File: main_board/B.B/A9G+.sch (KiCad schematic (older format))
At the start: 20 parts

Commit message: preparation_to_drawing_PCB
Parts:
- removed Q? (x2): Q_NMOS_DGS, Package_TO_SOT_SMD:SOT-23, symbol Device:Q_NMOS_DGS
- added Q? (x2): CJ3134K, Package_TO_SOT_SMD:SOT-23, symbol Transistor_FET:2N7002
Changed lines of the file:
@@
 Text HLabel 2150 3550 0    50   Input ~ 0
 PWR_KEY
-$Comp
-L Device:Q_NMOS_DGS Q?
-U 1 1 5F805096
-P 2100 2800
-F 0 "Q?" H 2306 2846 50  0000 L CNN
-F 1 "Q_NMOS_DGS" H 2306 2755 50  0000 L CNN
-F 2 "Package_TO_SOT_SMD:SOT-23" H 2300 2900 50  0001 C CNN
-F 3 "~" H 2100 2800 50  0001 C CNN
-	1    2100 2800
-	1    0    0    -1
-$EndComp
 Wire Wire Line
 	2200 2600 2200 2550
@@
 Text HLabel 3250 3050 0    50   Input ~ 0
 INT
-$Comp
-L Device:Q_NMOS_DGS Q?
-U 1 1 5F9775A3
-P 2350 3550
-F 0 "Q?" H 2556 3596 50  0000 L CNN
-F 1 "Q_NMOS_DGS" H 2556 3505 50  0000 L CNN
-F 2 "Package_TO_SOT_SMD:SOT-23" H 2550 3650 50  0001 C CNN
-F 3 "~" H 2350 3550 50  0001 C CNN
-	1    2350 3550
-	1    0    0    -1
-$EndComp
 Wire Wire Line
 	2450 3350 2450 2450
@@
 	1    0    0    -1
 $EndComp
+$Comp
+L Transistor_FET:2N7002 Q?
+U 1 1 5FAAADE2
+P 2350 3550
+AR Path="/5F77B818/5FAAADE2" Ref="Q?"  Part="1"
+AR Path="/5F9EE529/5F9AAC54/5FAAADE2" Ref="Q?"  Part="1"
+F 0 "Q?" H 2554 3596 50  0000 L CNN
+F 1 "CJ3134K" H 2554 3505 50  0000 L CNN
+F 2 "Package_TO_SOT_SMD:SOT-23" H 2550 3475 50  0001 L CIN
+F 3 "https://datasheet.lcsc.com/szlcsc/Changjiang-Electronics-Tech-CJ-CJ3134K_C110100.pdf" H 2350 3550 50  0001 L CNN
+F 4 "C110100" H 2350 3550 50  0001 C CNN "LCSC"
+F 5 "nutno vyměnit (musí být ->  Vgs-min>1.6V)" H 2350 3550 50  0001 C CNN "poznamka"
+	1    2350 3550
+	1    0    0    -1
+$EndComp
+$Comp
+L Transistor_FET:2N7002 Q?
+U 1 1 5FAACBD2
+P 2100 2800
+AR Path="/5F77B818/5FAACBD2" Ref="Q?"  Part="1"
+AR Path="/5F9EE529/5F9AAC54/5FAACBD2" Ref="Q?"  Part="1"
+F 0 "Q?" H 1950 2850 50  0000 L CNN
+F 1 "CJ3134K" H 1850 2950 50  0000 L CNN
+F 2 "Package_TO_SOT_SMD:SOT-23" H 2300 2725 50  0001 L CIN
+F 3 "https://datasheet.lcsc.com/szlcsc/Changjiang-Electronics-Tech-CJ-CJ3134K_C110100.pdf" H 2100 2800 50  0001 L CNN
+F 4 "C110100" H 2100 2800 50  0001 C CNN "LCSC"
+F 5 "nutno vyměnit (musí být ->  Vgs-min>1.6V)" H 2100 2800 50  0001 C CNN "poznamka"
+	1    2100 2800
+	1    0    0    -1
+$EndComp

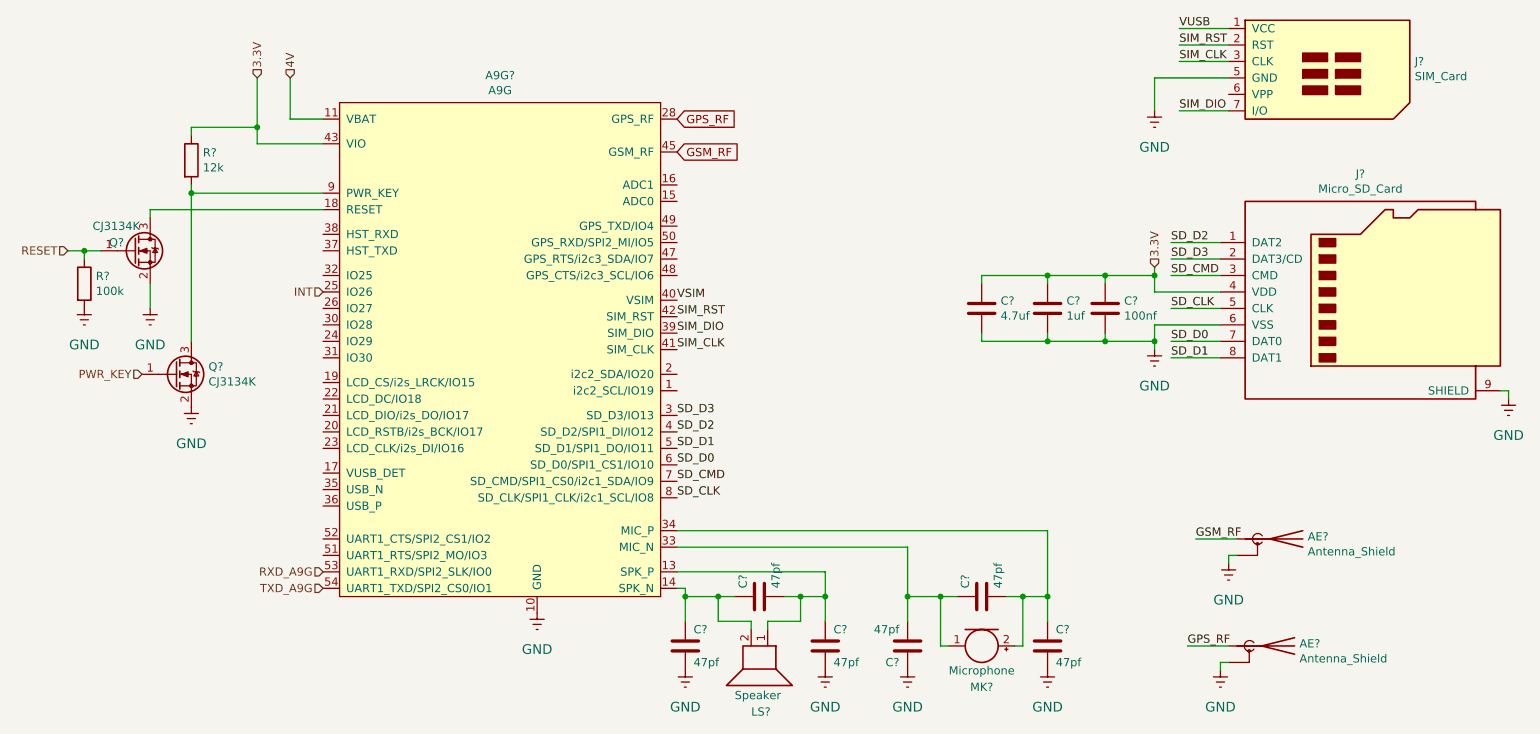
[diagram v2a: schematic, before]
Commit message: complete_preparation_to_drawing_PCB
footprint for all component and LCSC code for everything for mounting in JLCPCB
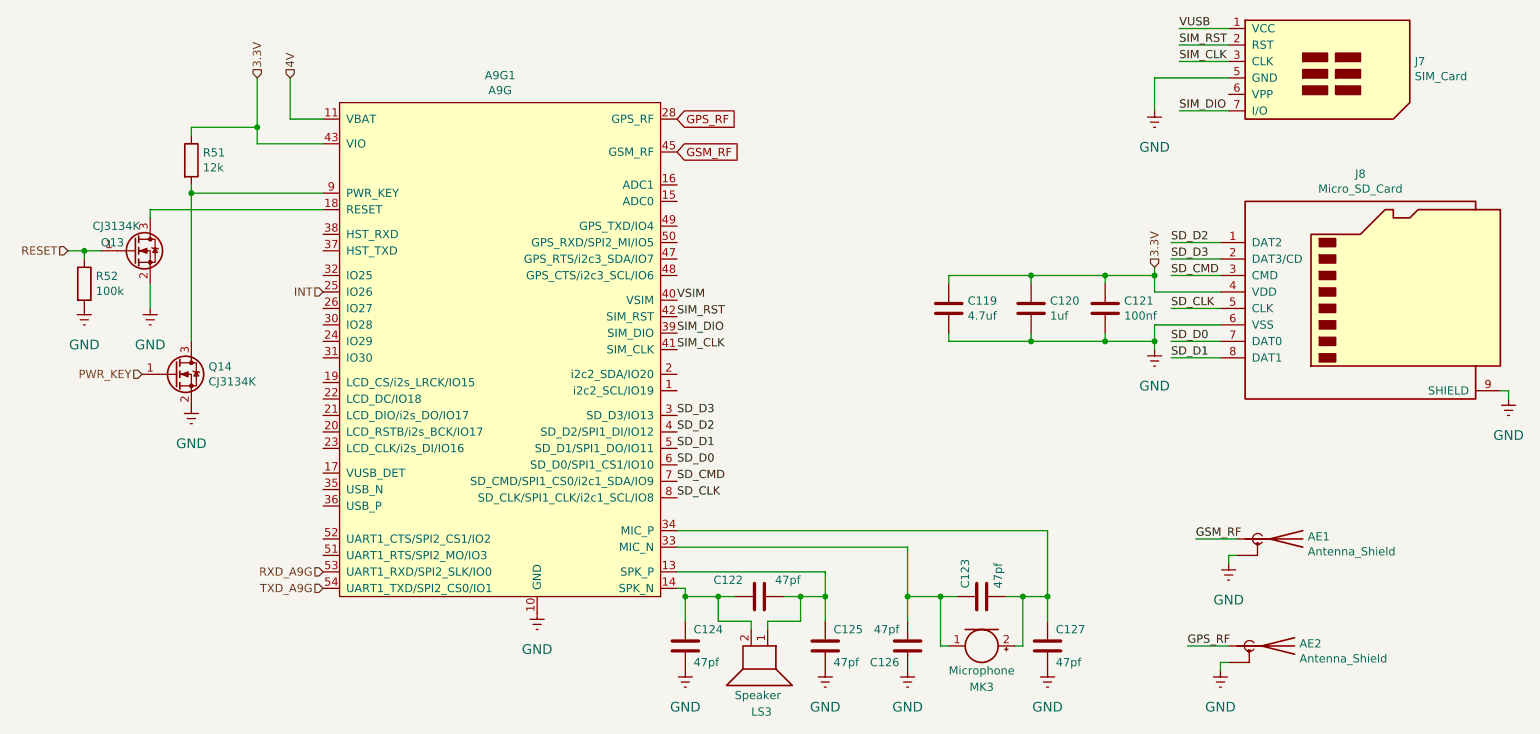
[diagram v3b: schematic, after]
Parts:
- A9G1: renamed from A9G?; footprint (none) -> BB:A9G
- AE1, AE2: renamed from AE?; footprint (none) -> BB:conn_antena; poznamka v0.2 = konektor později přímo anteéna -> v0.2 = konektor později přímo anténa
- C119: renamed from C?; LCSC (none) -> C19666
- C120: renamed from C?; LCSC (none) -> C15849
- C121: renamed from C?; LCSC (none) -> C57112
- J7: renamed from J?; footprint (none) -> BB:SIM
- J8: renamed from J?; footprint (none) -> BB:micro-SD
- LS3: renamed from LS?; footprint (none) -> Connector_PinHeader_2.54mm:PinHeader_1x02_P2.54mm_Vertical
- MK3: renamed from MK?; footprint (none) -> Connector_PinHeader_2.54mm:PinHeader_1x02_P2.54mm_Vertical
- gave numbers to parts that had none: 10
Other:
- moved on the sheet: C119, C120

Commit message: start vith pcb
firsxxt proposal component layout of main board
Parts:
- removed J7: SIM_Card, BB:SIM, symbol Connector:SIM_Card
- added J7: SIM_Card, BB:SIM, symbol B.B-rescue:SIM_Card
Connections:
- net SIM_CLK: now also J7.3 (CLK)
- net SIM_DIO: now also J7.6 (I/O)
- net SIM_RST: now also J7.2 (RST)
- net VUSB: now also J7.1 (VCC)
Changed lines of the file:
@@
 EESchema Schematic File Version 4
-LIBS:B.B-cache
-EELAYER 29 0
+EELAYER 30 0
 EELAYER END
 $Descr A4 11693 8268
@@
 F 3 "" H 4000 3800 50  0001 C CNN
 	1    4350 3500
-	1    0    0    -1
-$EndComp
-$Comp
-L Connector:SIM_Card J7
-U 1 1 5F7BD351
-P 9250 1750
-F 0 "J7" H 9880 1850 50  0000 L CNN
-F 1 "SIM_Card" H 9880 1759 50  0000 L CNN
-F 2 "BB:SIM" H 9250 2100 50  0001 C CNN
-F 3 "https://www.we-online.de/katalog/datasheet/693010010601.pdf" H 9200 1750 50  0001 C CNN
-	1    9250 1750
 	1    0    0    -1
 $EndComp
@@
 Connection ~ 8000 2950
 Connection ~ 8000 3350
+$Comp
+L B.B-rescue:SIM_Card J7
+U 1 1 5FAC315F
+P 9250 1750
+F 0 "J7" H 9880 1850 50  0000 L CNN
+F 1 "SIM_Card" H 9880 1759 50  0000 L CNN
+F 2 "BB:SIM" H 9250 2100 50  0001 C CNN
+F 3 "https://www.we-online.de/katalog/datasheet/693010010601.pdf" H 9200 1750 50  0001 C CNN
+	1    9250 1750
+	1    0    0    -1
+$EndComp
 $EndSCHEMATC
